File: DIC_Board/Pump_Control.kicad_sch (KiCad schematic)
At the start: 0 parts

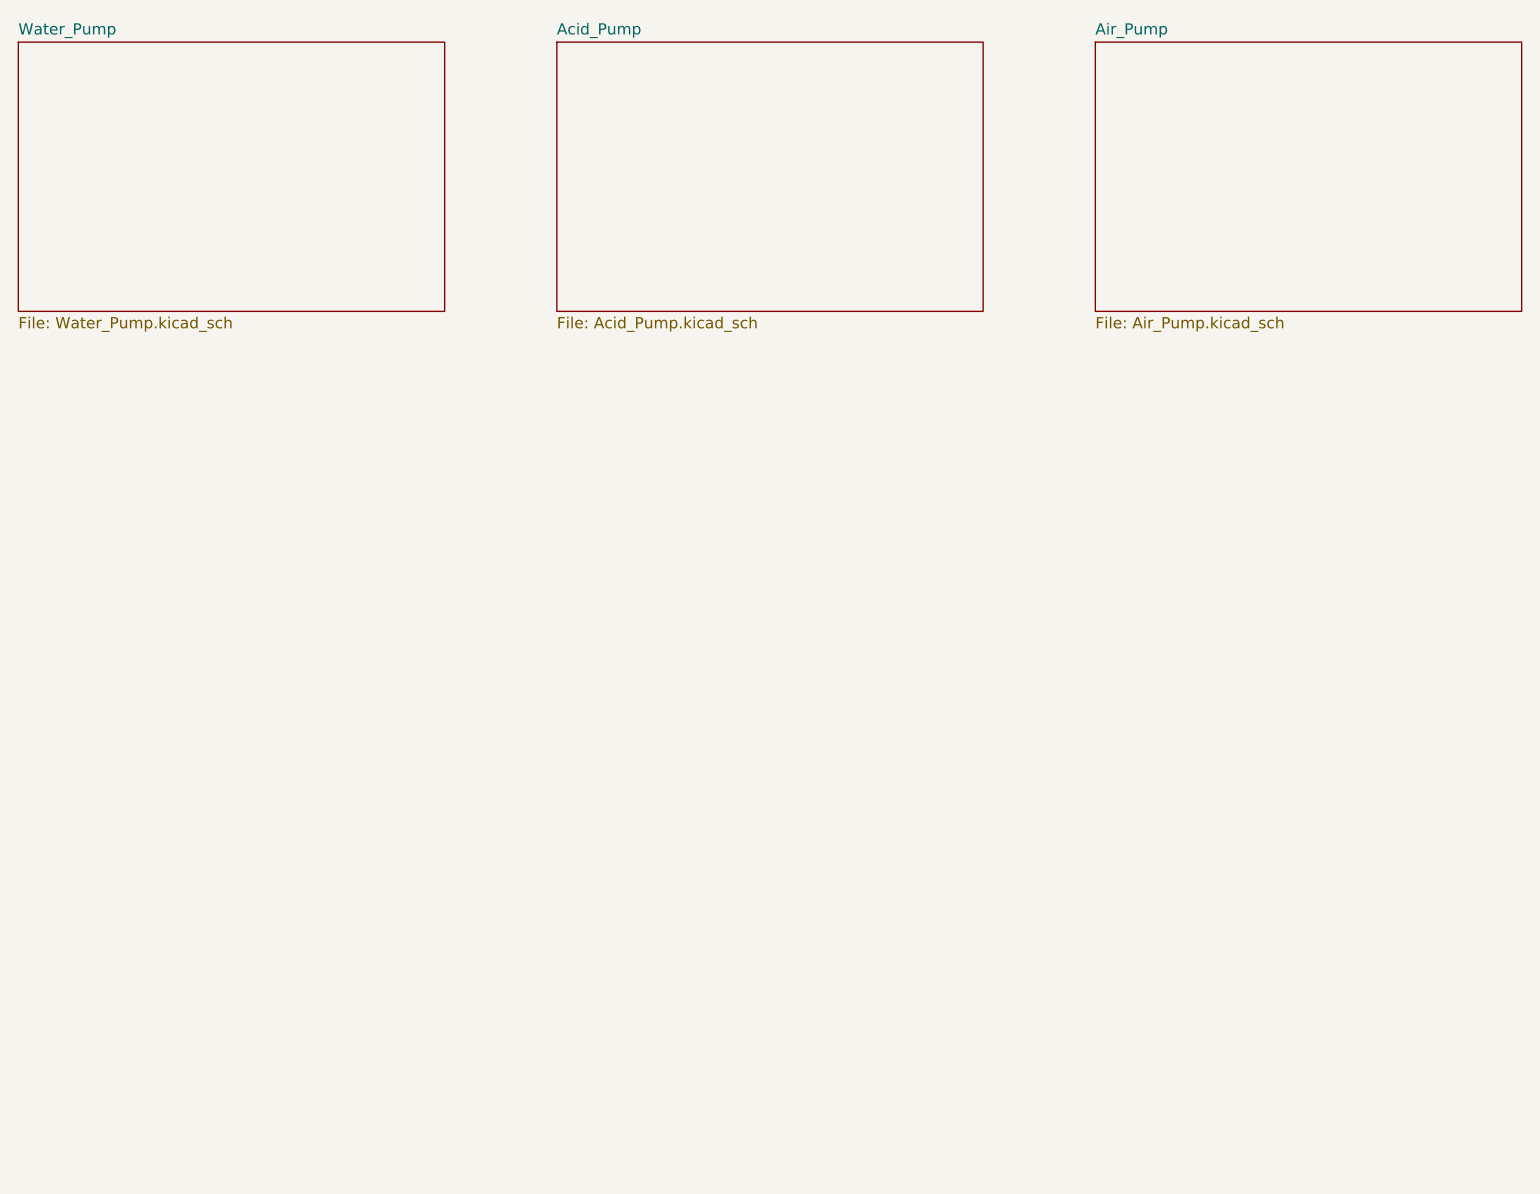
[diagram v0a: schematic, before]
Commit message: Completed water pump and added the 2.7V rail
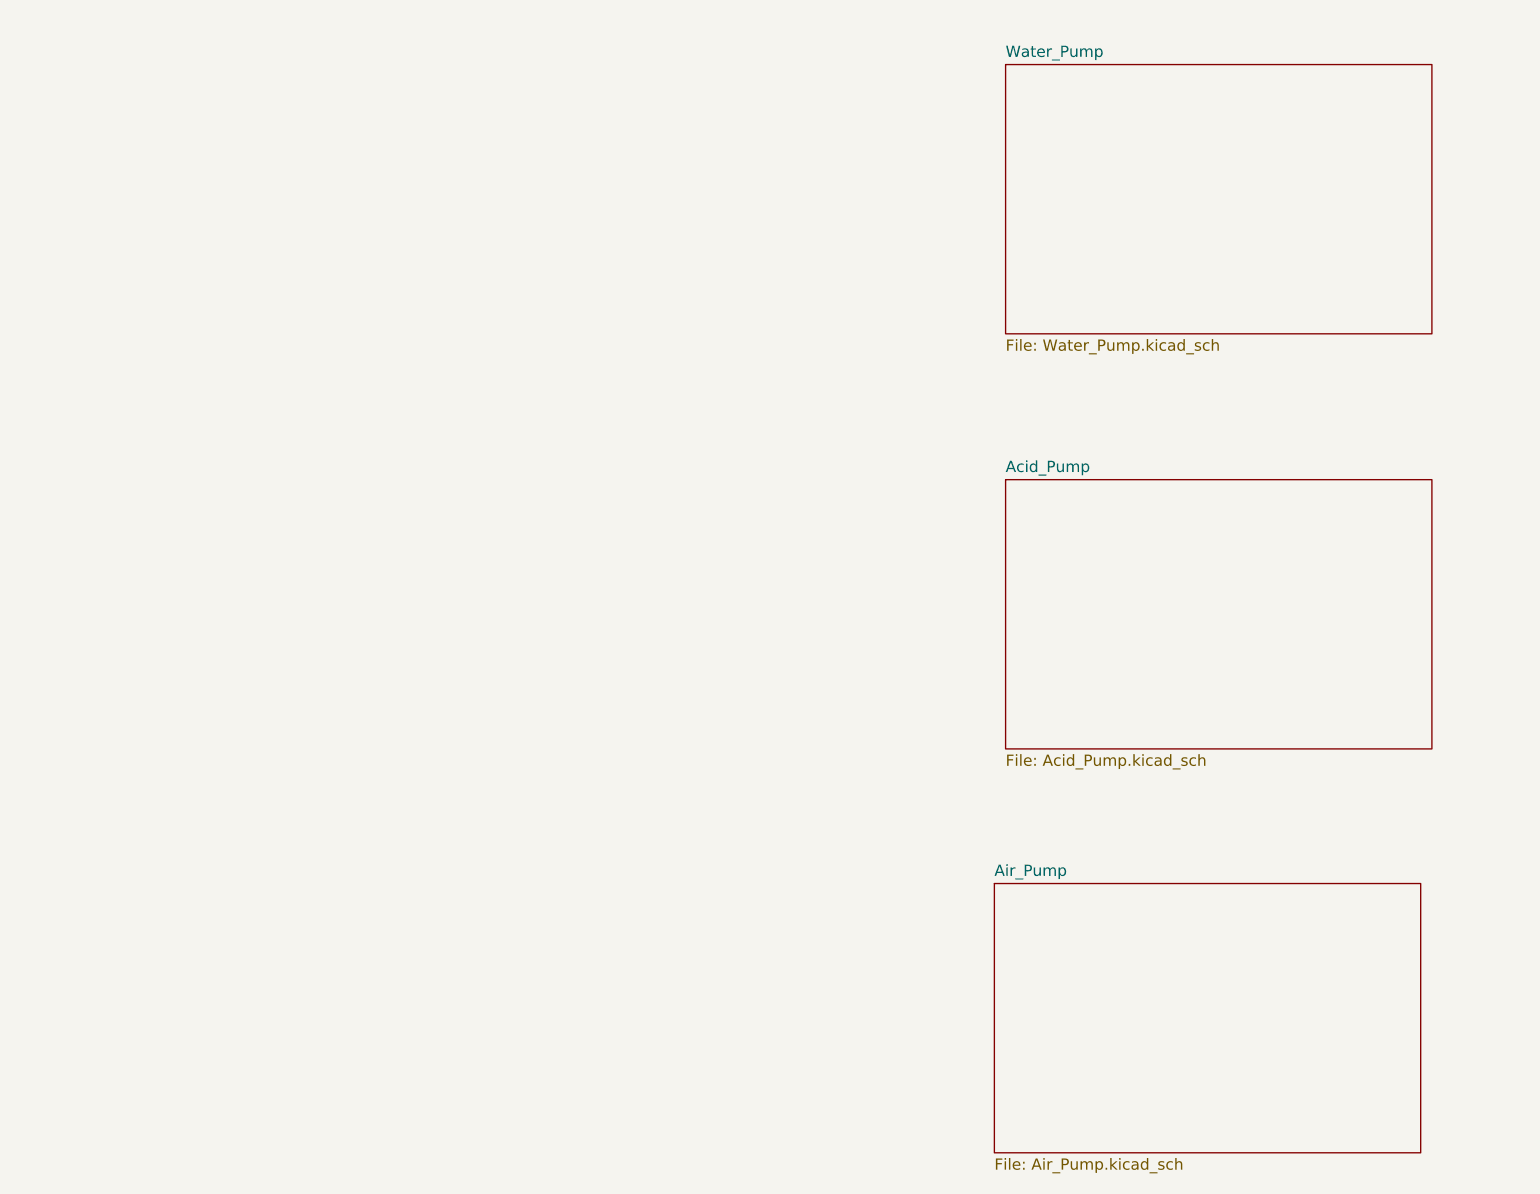
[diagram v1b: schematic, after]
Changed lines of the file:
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@@
 	)
 	(sheet
-		(at 25.4 25.4)
+		(at 137.16 27.94)
 		(size 48.26 30.48)
 		(exclude_from_sim no)
@@
 		)
 		(property "Sheetname" "Water_Pump"
-			(at 25.4 24.6884 0)
+			(at 137.16 27.2284 0)
 			(show_name no)
 			(do_not_autoplace no)
@@
 		)
 		(property "Sheetfile" "Water_Pump.kicad_sch"
-			(at 25.4 56.4646 0)
+			(at 137.16 59.0046 0)
 			(show_name no)
 			(do_not_autoplace no)
@@
 	)
 	(sheet
-		(at 86.36 25.4)
+		(at 135.89 120.65)
+		(size 48.26 30.48)
+		(exclude_from_sim no)
+		(in_bom yes)
+		(on_board yes)
+		(dnp no)
+		(fields_autoplaced yes)
+		(stroke
+			(width 0.1524)
+			(type solid)
+		)
+		(fill
+			(color 0 0 0 0)
+		)
+		(property "Sheetname" "Air_Pump"
+			(at 135.89 119.9384 0)
+			(show_name no)
+			(do_not_autoplace no)
+			(effects
+				(font
+					(size 1.27 1.27)
+				)
+				(justify left bottom)
+			)
+		)
+		(property "Sheetfile" "Air_Pump.kicad_sch"
+			(at 135.89 151.7146 0)
+			(show_name no)
+			(do_not_autoplace no)
+			(effects
+				(font
+					(size 1.27 1.27)
+				)
+				(justify left top)
+			)
+		)
+		(instances
+			(project "DIC_Board"
+				(path "/bb0ef0df-c181-443a-843c-695cd2e0efee/c0c341f0-cc08-4486-9fa7-67c0e9d2ea1a"
+					(page "11")
+				)
+			)
+		)
+	)
+	(sheet
+		(at 137.16 74.93)
 		(size 48.26 30.48)
 		(exclude_from_sim no)
@@
 		)
 		(property "Sheetname" "Acid_Pump"
-			(at 86.36 24.6884 0)
+			(at 137.16 74.2184 0)
 			(show_name no)
 			(do_not_autoplace no)
@@
 		)
 		(property "Sheetfile" "Acid_Pump.kicad_sch"
-			(at 86.36 56.4646 0)
+			(at 137.16 105.9946 0)
 			(show_name no)
 			(do_not_autoplace no)
@@
 		)
 	)
-	(sheet
-		(at 147.32 25.4)
-		(size 48.26 30.48)
-		(exclude_from_sim no)
-		(in_bom yes)
-		(on_board yes)
-		(dnp no)
-		(fields_autoplaced yes)
-		(stroke
-			(width 0.1524)
-			(type solid)
-		)
-		(fill
-			(color 0 0 0 0)
-		)
-		(property "Sheetname" "Air_Pump"
-			(at 147.32 24.6884 0)
-			(show_name no)
-			(do_not_autoplace no)
-			(effects
-				(font
-					(size 1.27 1.27)
-				)
-				(justify left bottom)
-			)
-		)
-		(property "Sheetfile" "Air_Pump.kicad_sch"
-			(at 147.32 56.4646 0)
-			(show_name no)
-			(do_not_autoplace no)
-			(effects
-				(font
-					(size 1.27 1.27)
-				)
-				(justify left top)
-			)
-		)
-		(instances
-			(project "DIC_Board"
-				(path "/bb0ef0df-c181-443a-843c-695cd2e0efee/c0c341f0-cc08-4486-9fa7-67c0e9d2ea1a"
-					(page "11")
-				)
-			)
-		)
-	)
-	(embedded_fonts no)
 )

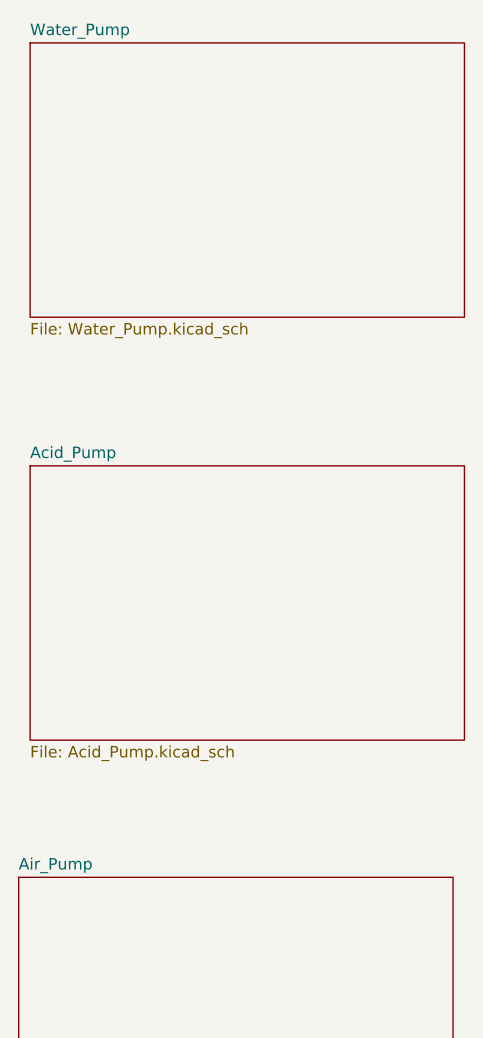
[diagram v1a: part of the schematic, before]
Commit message: Separated the power sheets, did the sensor sheets.
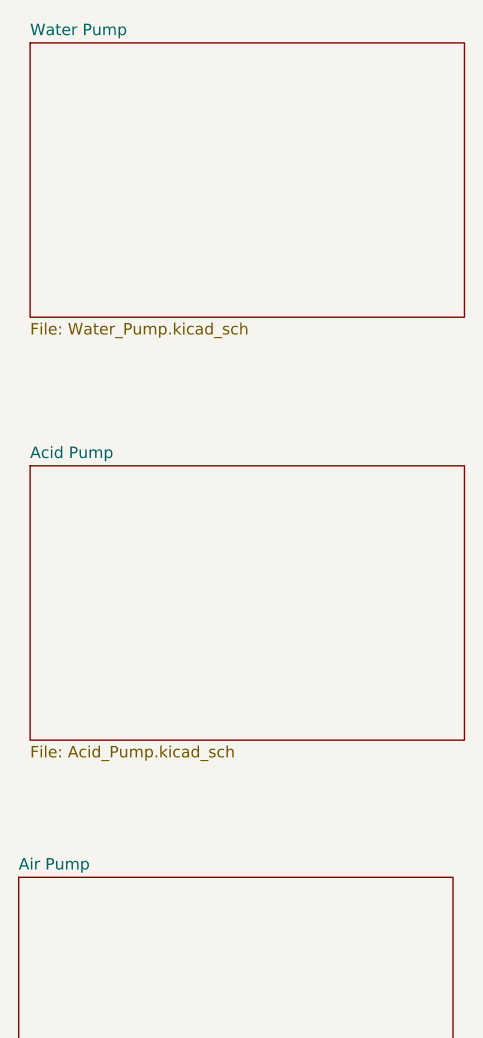
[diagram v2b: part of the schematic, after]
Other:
- sheet Acid_Pump renamed Acid Pump
- sheet Air_Pump renamed Air Pump
- sheet Water_Pump renamed Water Pump
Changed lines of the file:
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@@
 			(color 0 0 0 0)
 		)
-		(property "Sheetname" "Water_Pump"
+		(property "Sheetname" "Water Pump"
 			(at 137.16 27.2284 0)
 			(show_name no)
@@
 			(color 0 0 0 0)
 		)
-		(property "Sheetname" "Air_Pump"
+		(property "Sheetname" "Air Pump"
 			(at 135.89 119.9384 0)
 			(show_name no)
@@
 			(color 0 0 0 0)
 		)
-		(property "Sheetname" "Acid_Pump"
+		(property "Sheetname" "Acid Pump"
 			(at 137.16 74.2184 0)
 			(show_name no)

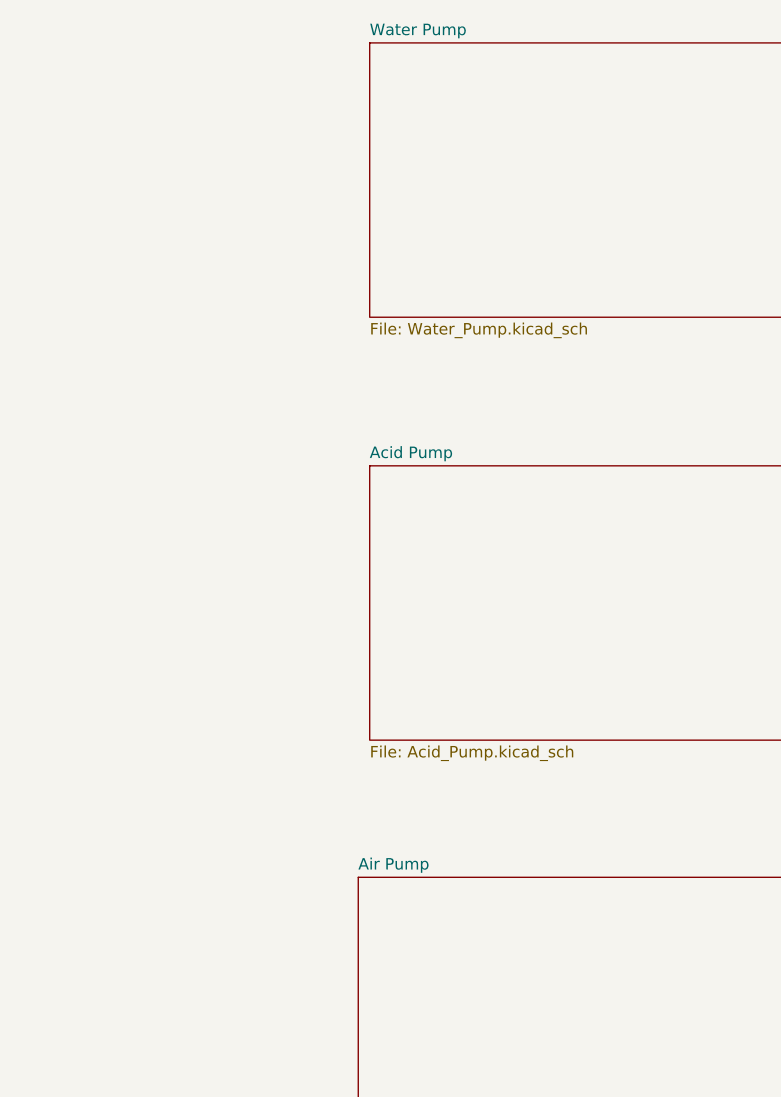
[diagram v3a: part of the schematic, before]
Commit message: Synchronize schematic hierarchy and MCU pin map
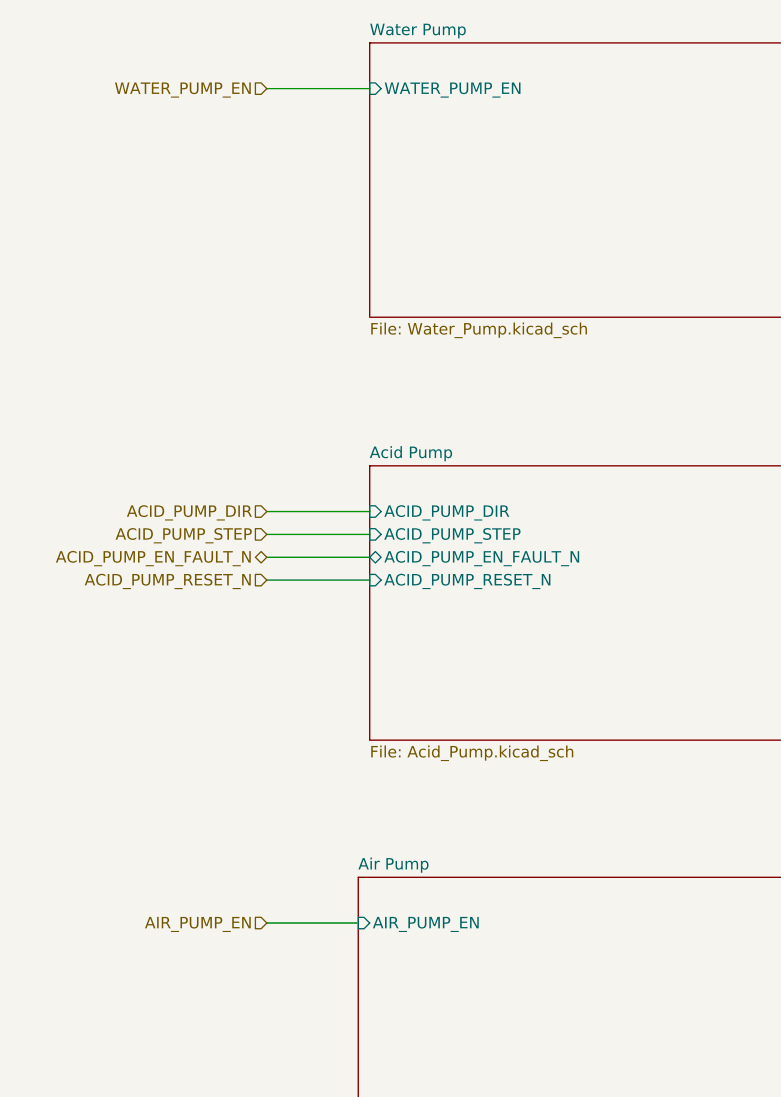
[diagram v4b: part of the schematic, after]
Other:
- sheet Acid Pump ports: added ACID_PUMP_DIR, ACID_PUMP_EN_FAULT_N, ACID_PUMP_RESET_N, ACID_PUMP_STEP; removed none
- sheet Air Pump ports: added AIR_PUMP_EN; removed none
- sheet Water Pump ports: added WATER_PUMP_EN; removed none
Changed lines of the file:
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@@
 		(title "Pump Control")
+	)
+	(wire
+		(pts
+			(xy 125.73 33.02) (xy 137.16 33.02)
+		)
+		(stroke
+			(width 0)
+			(type default)
+		)
+	)
+	(wire
+		(pts
+			(xy 125.73 80.01) (xy 137.16 80.01)
+		)
+		(stroke
+			(width 0)
+			(type default)
+		)
+	)
+	(wire
+		(pts
+			(xy 125.73 82.55) (xy 137.16 82.55)
+		)
+		(stroke
+			(width 0)
+			(type default)
+		)
+	)
+	(wire
+		(pts
+			(xy 125.73 85.09) (xy 137.16 85.09)
+		)
+		(stroke
+			(width 0)
+			(type default)
+		)
+	)
+	(wire
+		(pts
+			(xy 125.73 87.63) (xy 137.16 87.63)
+		)
+		(stroke
+			(width 0)
+			(type default)
+		)
+	)
+	(wire
+		(pts
+			(xy 125.73 125.73) (xy 135.89 125.73)
+		)
+		(stroke
+			(width 0)
+			(type default)
+		)
+	)
+	(hierarchical_label "WATER_PUMP_EN"
+		(shape input)
+		(at 125.73 33.02 180)
+		(effects
+			(font
+				(size 1.27 1.27)
+			)
+			(justify right)
+		)
+	)
+	(hierarchical_label "ACID_PUMP_DIR"
+		(shape input)
+		(at 125.73 80.01 180)
+		(effects
+			(font
+				(size 1.27 1.27)
+			)
+			(justify right)
+		)
+	)
+	(hierarchical_label "ACID_PUMP_STEP"
+		(shape input)
+		(at 125.73 82.55 180)
+		(effects
+			(font
+				(size 1.27 1.27)
+			)
+			(justify right)
+		)
+	)
+	(hierarchical_label "ACID_PUMP_EN_FAULT_N"
+		(shape bidirectional)
+		(at 125.73 85.09 180)
+		(effects
+			(font
+				(size 1.27 1.27)
+			)
+			(justify right)
+		)
+	)
+	(hierarchical_label "ACID_PUMP_RESET_N"
+		(shape input)
+		(at 125.73 87.63 180)
+		(effects
+			(font
+				(size 1.27 1.27)
+			)
+			(justify right)
+		)
+	)
+	(hierarchical_label "AIR_PUMP_EN"
+		(shape input)
+		(at 125.73 125.73 180)
+		(effects
+			(font
+				(size 1.27 1.27)
+			)
+			(justify right)
+		)
 	)
 	(sheet
@@
 			)
 		)
+		(pin "WATER_PUMP_EN" input
+			(at 137.16 33.02 180)
+			(effects
+				(font
+					(size 1.27 1.27)
+				)
+				(justify left)
+			)
+		)
 		(instances
 			(project "DIC_Board"
@@
 			)
 		)
+		(pin "AIR_PUMP_EN" input
+			(at 135.89 125.73 180)
+			(effects
+				(font
+					(size 1.27 1.27)
+				)
+				(justify left)
+			)
+		)
 		(instances
 			(project "DIC_Board"
@@
 			)
 		)
+		(pin "ACID_PUMP_DIR" input
+			(at 137.16 80.01 180)
+			(effects
+				(font
+					(size 1.27 1.27)
+				)
+				(justify left)
+			)
+		)
+		(pin "ACID_PUMP_STEP" input
+			(at 137.16 82.55 180)
+			(effects
+				(font
+					(size 1.27 1.27)
+				)
+				(justify left)
+			)
+		)
+		(pin "ACID_PUMP_EN_FAULT_N" bidirectional
+			(at 137.16 85.09 180)
+			(effects
+				(font
+					(size 1.27 1.27)
+				)
+				(justify left)
+			)
+		)
+		(pin "ACID_PUMP_RESET_N" input
+			(at 137.16 87.63 180)
+			(effects
+				(font
+					(size 1.27 1.27)
+				)
+				(justify left)
+			)
+		)
